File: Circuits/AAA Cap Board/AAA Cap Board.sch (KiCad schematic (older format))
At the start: 18 parts

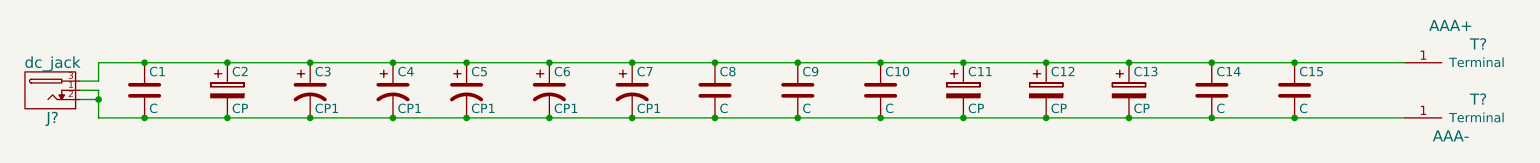
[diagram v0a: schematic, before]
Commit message: Circuits: Moving Kicad Parts to a common directory
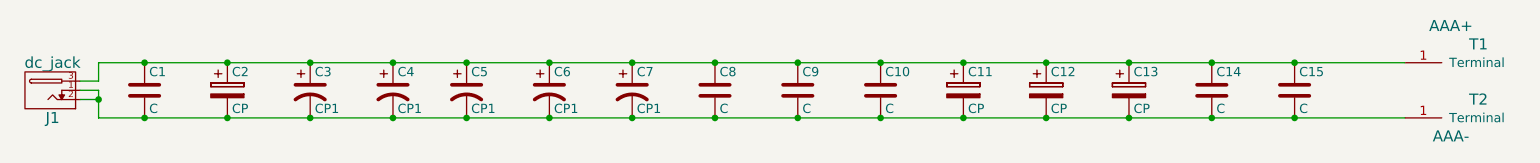
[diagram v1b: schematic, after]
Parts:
- gave numbers to parts that had none: 3
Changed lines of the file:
@@
 LIBS:w_device
 LIBS:aaa_terminal
+LIBS:AAA Cap Board-cache
 EELAYER 25 0
 EELAYER END
@@
 $EndComp
 $Comp
-L dc_jack J?
+L dc_jack J1
 U 1 1 5650153A
 P 2100 3100
-F 0 "J?" H 2100 3250 60  0000 C CNN
+F 0 "J1" H 2100 3250 60  0000 C CNN
 F 1 "dc_jack" H 2100 2950 60  0000 C CNN
 F 2 "" H 2100 3100 60  0000 C CNN
@@
 $EndComp
 $Comp
-L AAA_Terminal T?
+L AAA_Terminal T1
 U 1 1 565016B7
 P 10000 2950
-F 0 "T?" V 9900 2800 60  0000 C CNN
+F 0 "T1" V 9900 2800 60  0000 C CNN
 F 1 "AAA+" V 9800 2650 60  0000 C CNN
 F 2 "" H 10000 2950 60  0000 C CNN
@@
 $EndComp
 $Comp
-L AAA_Terminal T?
+L AAA_Terminal T2
 U 1 1 565017EB
 P 10000 3250
-F 0 "T?" V 9900 3100 60  0000 C CNN
+F 0 "T2" V 9900 3100 60  0000 C CNN
 F 1 "AAA-" V 10100 2950 60  0000 C CNN
 F 2 "" H 10000 3250 60  0000 C CNN

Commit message: Circuits: Updating AAA Cap Board PCB
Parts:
- C1: footprint (none) -> Capacitors_SMD:C_0603_HandSoldering
- C10: footprint (none) -> Capacitors_SMD:C_1210_HandSoldering
- C11: footprint (none) -> Capacitors_ThroughHole:C_Rect_L13_W6_H12_P10
- C12: footprint (none) -> Capacitors_ThroughHole:C_Rect_L18_W6_H12_P15
- C13: footprint (none) -> Capacitors_ThroughHole:C_Rect_L18_W9_H15_P15
- C14: footprint (none) -> Capacitors_ThroughHole:C_Disc_D3_P2.5
- C15: footprint (none) -> Capacitors_ThroughHole:C_Disc_D7.5_P5
- C2: footprint (none) -> Capacitors_ThroughHole:C_Rect_L7.5_W6.5_P5
- C3: footprint (none) -> Capacitors_ThroughHole:C_Radial_D10_L13_P5
- C4: footprint (none) -> Capacitors_ThroughHole:C_Radial_D10_L16_P5
- C5: footprint (none) -> Capacitors_ThroughHole:C_Radial_D12.5_L25_P5
- C6: footprint (none) -> Capacitors_ThroughHole:C_Radial_D14_L25_P5
- C7: footprint (none) -> Capacitors_ThroughHole:C_Radial_D18_L36_P7.5
- C8: footprint (none) -> Capacitors_SMD:C_0805_HandSoldering
- C9: footprint (none) -> Capacitors_SMD:C_1206_HandSoldering
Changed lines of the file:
@@
 F 0 "C14" H 8425 3200 50  0000 L CNN
 F 1 "C" H 8425 3000 50  0000 L CNN
-F 2 "" H 8438 2950 30  0000 C CNN
+F 2 "Capacitors_ThroughHole:C_Disc_D3_P2.5" H 8438 2950 30  0001 C CNN
 F 3 "" H 8400 3100 60  0000 C CNN
 	1    8400 3100
@@
 F 0 "C10" H 6625 3200 50  0000 L CNN
 F 1 "C" H 6625 3000 50  0000 L CNN
-F 2 "" H 6638 2950 30  0000 C CNN
+F 2 "Capacitors_SMD:C_1210_HandSoldering" H 6638 2950 30  0001 C CNN
 F 3 "" H 6600 3100 60  0000 C CNN
 	1    6600 3100
@@
 F 0 "C9" H 6175 3200 50  0000 L CNN
 F 1 "C" H 6175 3000 50  0000 L CNN
-F 2 "" H 6188 2950 30  0000 C CNN
+F 2 "Capacitors_SMD:C_1206_HandSoldering" H 6188 2950 30  0001 C CNN
 F 3 "" H 6150 3100 60  0000 C CNN
 	1    6150 3100
@@
 F 0 "C8" H 5725 3200 50  0000 L CNN
 F 1 "C" H 5725 3000 50  0000 L CNN
-F 2 "" H 5738 2950 30  0000 C CNN
+F 2 "Capacitors_SMD:C_0805_HandSoldering" H 5738 2950 30  0001 C CNN
 F 3 "" H 5700 3100 60  0000 C CNN
 	1    5700 3100
@@
 F 0 "C1" H 2625 3200 50  0000 L CNN
 F 1 "C" H 2625 3000 50  0000 L CNN
-F 2 "" H 2638 2950 30  0000 C CNN
+F 2 "Capacitors_SMD:C_0603_HandSoldering" H 2638 2950 30  0001 C CNN
 F 3 "" H 2600 3100 60  0000 C CNN
 	1    2600 3100
@@
 F 0 "C13" H 7975 3200 50  0000 L CNN
 F 1 "CP" H 7975 3000 50  0000 L CNN
-F 2 "" H 7988 2950 30  0000 C CNN
+F 2 "Capacitors_ThroughHole:C_Rect_L18_W9_H15_P15" H 7988 2950 30  0001 C CNN
 F 3 "" H 7950 3100 60  0000 C CNN
 	1    7950 3100
@@
 F 0 "C12" H 7525 3200 50  0000 L CNN
 F 1 "CP" H 7525 3000 50  0000 L CNN
-F 2 "" H 7538 2950 30  0000 C CNN
+F 2 "Capacitors_ThroughHole:C_Rect_L18_W6_H12_P15" H 7538 2950 30  0001 C CNN
 F 3 "" H 7500 3100 60  0000 C CNN
 	1    7500 3100
@@
 F 0 "C11" H 7075 3200 50  0000 L CNN
 F 1 "CP" H 7075 3000 50  0000 L CNN
-F 2 "" H 7088 2950 30  0000 C CNN
+F 2 "Capacitors_ThroughHole:C_Rect_L13_W6_H12_P10" H 7088 2950 30  0001 C CNN
 F 3 "" H 7050 3100 60  0000 C CNN
 	1    7050 3100
@@
 F 0 "C2" H 3075 3200 50  0000 L CNN
 F 1 "CP" H 3075 3000 50  0000 L CNN
-F 2 "" H 3088 2950 30  0000 C CNN
+F 2 "Capacitors_ThroughHole:C_Rect_L7.5_W6.5_P5" H 3088 2950 30  0001 C CNN
 F 3 "" H 3050 3100 60  0000 C CNN
 	1    3050 3100
@@
 F 0 "C7" H 5275 3200 50  0000 L CNN
 F 1 "CP1" H 5275 3000 50  0000 L CNN
-F 2 "" H 5250 3100 60  0000 C CNN
+F 2 "Capacitors_ThroughHole:C_Radial_D18_L36_P7.5" H 5250 3100 60  0001 C CNN
 F 3 "" H 5250 3100 60  0000 C CNN
 	1    5250 3100
@@
 F 0 "C6" H 4825 3200 50  0000 L CNN
 F 1 "CP1" H 4825 3000 50  0000 L CNN
-F 2 "" H 4800 3100 60  0000 C CNN
+F 2 "Capacitors_ThroughHole:C_Radial_D14_L25_P5" H 4800 3100 60  0001 C CNN
 F 3 "" H 4800 3100 60  0000 C CNN
 	1    4800 3100
@@
 F 0 "C5" H 4375 3200 50  0000 L CNN
 F 1 "CP1" H 4375 3000 50  0000 L CNN
-F 2 "" H 4350 3100 60  0000 C CNN
+F 2 "Capacitors_ThroughHole:C_Radial_D12.5_L25_P5" H 4350 3100 60  0001 C CNN
 F 3 "" H 4350 3100 60  0000 C CNN
 	1    4350 3100
@@
 F 0 "C4" H 3975 3200 50  0000 L CNN
 F 1 "CP1" H 3975 3000 50  0000 L CNN
-F 2 "" H 3950 3100 60  0000 C CNN
+F 2 "Capacitors_ThroughHole:C_Radial_D10_L16_P5" H 3950 3100 60  0001 C CNN
 F 3 "" H 3950 3100 60  0000 C CNN
 	1    3950 3100
@@
 F 0 "C3" H 3525 3200 50  0000 L CNN
 F 1 "CP1" H 3525 3000 50  0000 L CNN
-F 2 "" H 3500 3100 60  0000 C CNN
+F 2 "Capacitors_ThroughHole:C_Radial_D10_L13_P5" H 3500 3100 60  0001 C CNN
 F 3 "" H 3500 3100 60  0000 C CNN
 	1    3500 3100
@@
 F 0 "C15" H 8875 3200 50  0000 L CNN
 F 1 "C" H 8875 3000 50  0000 L CNN
-F 2 "" H 8888 2950 30  0000 C CNN
+F 2 "Capacitors_ThroughHole:C_Disc_D7.5_P5" H 8888 2950 30  0001 C CNN
 F 3 "" H 8850 3100 60  0000 C CNN
 	1    8850 3100
@@
 F 0 "J1" H 2100 3250 60  0000 C CNN
 F 1 "dc_jack" H 2100 2950 60  0000 C CNN
-F 2 "" H 2100 3100 60  0000 C CNN
+F 2 "" H 2100 3100 60  0001 C CNN
 F 3 "" H 2100 3100 60  0000 C CNN
 	1    2100 3100
@@
 F 0 "T1" V 9900 2800 60  0000 C CNN
 F 1 "AAA+" V 9800 2650 60  0000 C CNN
-F 2 "" H 10000 2950 60  0000 C CNN
+F 2 "" H 10000 2950 60  0001 C CNN
 F 3 "" H 10000 2950 60  0000 C CNN
 	1    10000 2950
@@
 F 0 "T2" V 9900 3100 60  0000 C CNN
 F 1 "AAA-" V 10100 2950 60  0000 C CNN
-F 2 "" H 10000 3250 60  0000 C CNN
+F 2 "" H 10000 3250 60  0001 C CNN
 F 3 "" H 10000 3250 60  0000 C CNN
 	1    10000 3250
